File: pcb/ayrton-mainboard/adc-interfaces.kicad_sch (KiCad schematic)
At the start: 1 part, among them U2 XC7K160T-2FFG676C

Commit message: Continued initial system design
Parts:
- removed U2: XC7K160T-2FFG676C, symbol xilinx-azonenberg:XC7KxT-FFG676
- added U2: XC7K160T-2FFG676C, symbol xilinx-azonenberg:XC7KxT-FFG676
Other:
- removed sheet FPGA DDR3 SODIMM
- removed sheet FPGA power

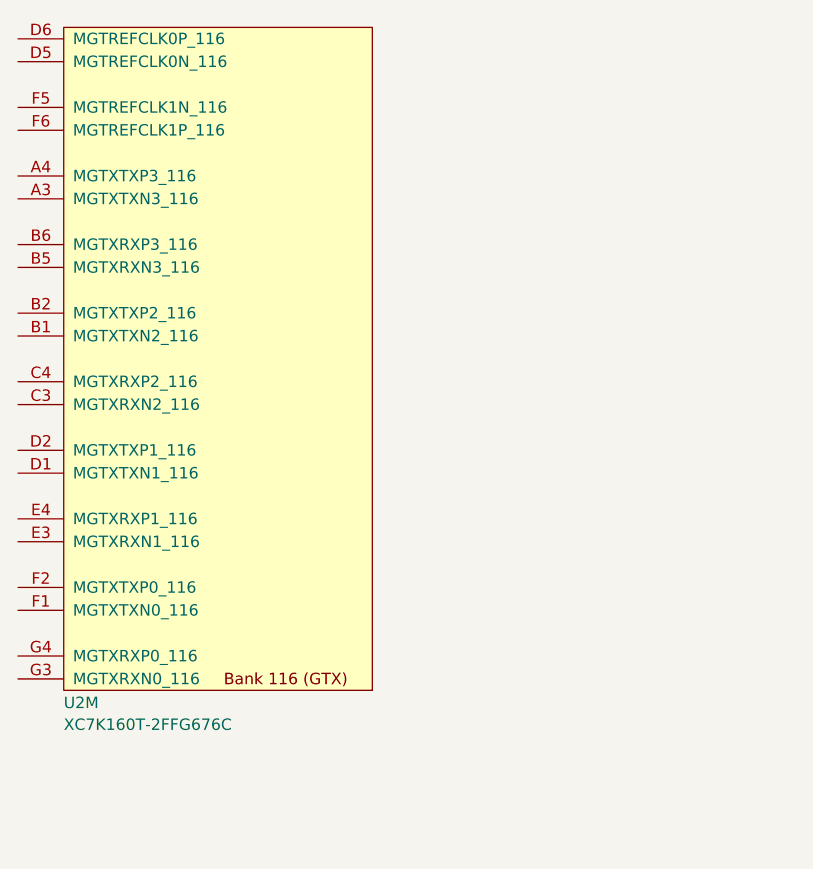
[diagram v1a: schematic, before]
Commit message: Continued initial schematic, working on LPDDR4
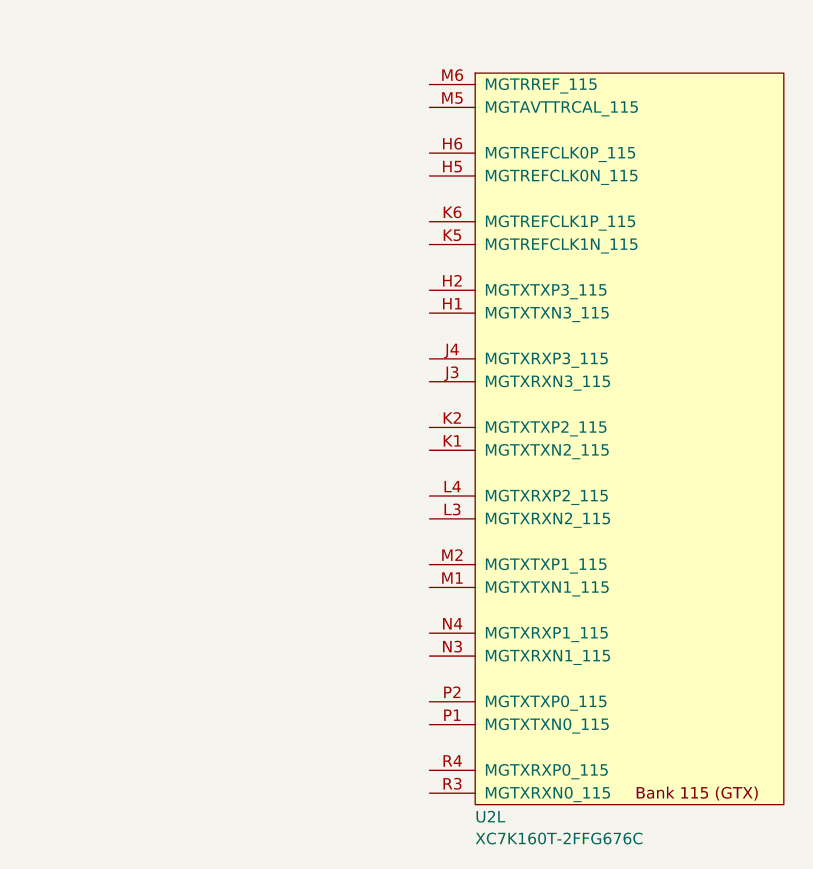
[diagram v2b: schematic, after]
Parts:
- removed U2: XC7K160T-2FFG676C, symbol xilinx-azonenberg:XC7KxT-FFG676
- added U2: XC7K160T-2FFG676C, symbol xilinx-azonenberg:XC7KxT-FFG676
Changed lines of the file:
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@@
 	(generator "eeschema")
 	(generator_version "8.0")
-	(paper "A4")
+	(paper "A3")
 	(title_block
 		(title "AYRTON Main Board")
-		(date "2024-11-18")
+		(date "2024-11-21")
 		(rev "0.1")
 		(company "Antikernel Labs")
@@
 	(symbol
 		(lib_id "xilinx-azonenberg:XC7KxT-FFG676")
-		(at 66.04 115.57 0)
-		(unit 13)
+		(at 111.76 128.27 0)
+		(unit 12)
 		(exclude_from_sim no)
 		(in_bom yes)
@@
 		(dnp no)
 		(property "Reference" "U2"
-			(at 66.04 116.9557 0)
+			(at 111.76 129.6557 0)
 			(effects
 				(font
@@
 		)
 		(property "Value" "XC7K160T-2FFG676C"
-			(at 66.04 119.38 0)
+			(at 111.76 132.08 0)
 			(effects
 				(font
@@
 		)
 		(property "Footprint" ""
-			(at 66.04 115.57 0)
+			(at 111.76 128.27 0)
 			(effects
 				(font
@@
 		)
 		(property "Datasheet" ""
-			(at 66.04 115.57 0)
+			(at 111.76 128.27 0)
 			(effects
 				(font
@@
 		)
 		(property "Description" ""
-			(at 66.04 115.57 0)
+			(at 111.76 128.27 0)
 			(effects
 				(font
@@
 				(path "/11b16c18-86a9-45f7-bd03-4e81057d99ff/f6fa3d68-580e-4966-a5d1-759c191a1b84"
 					(reference "U2")
-					(unit 13)
+					(unit 12)
 				)
 			)
